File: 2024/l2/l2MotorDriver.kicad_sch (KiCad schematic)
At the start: 17 parts, among them J4 Conn_01x02, J5 Conn_01x02, J6 Conn_01x02, J7 Conn_01x02, Q1 IRF540N, Q2 IRF540N, Q3 IRF540N, Q4 IRF540N, SW1 SW_SPDT, U1 VNH5019A-E, U2 VNH5019A-E, U3 VNH5019A-E, U4 VNH5019A-E

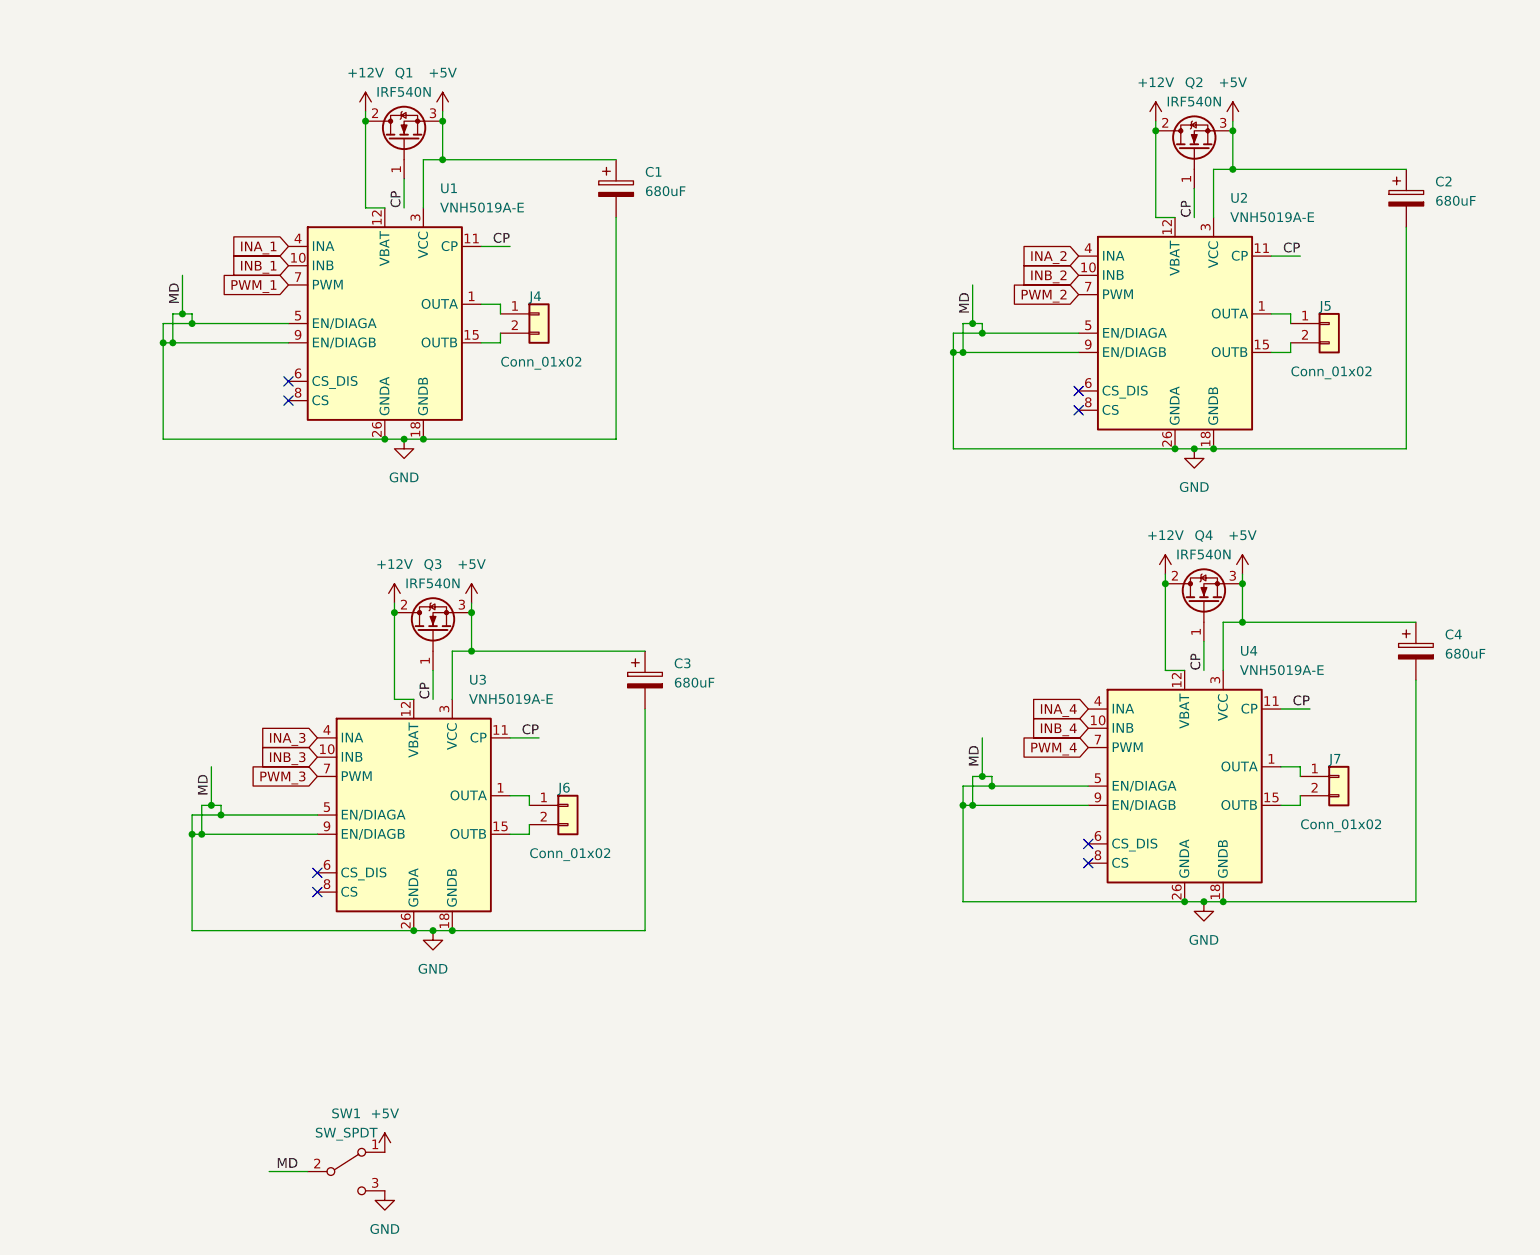
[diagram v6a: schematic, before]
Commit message: 5/9 final
fixed the problem with motor driver schematics
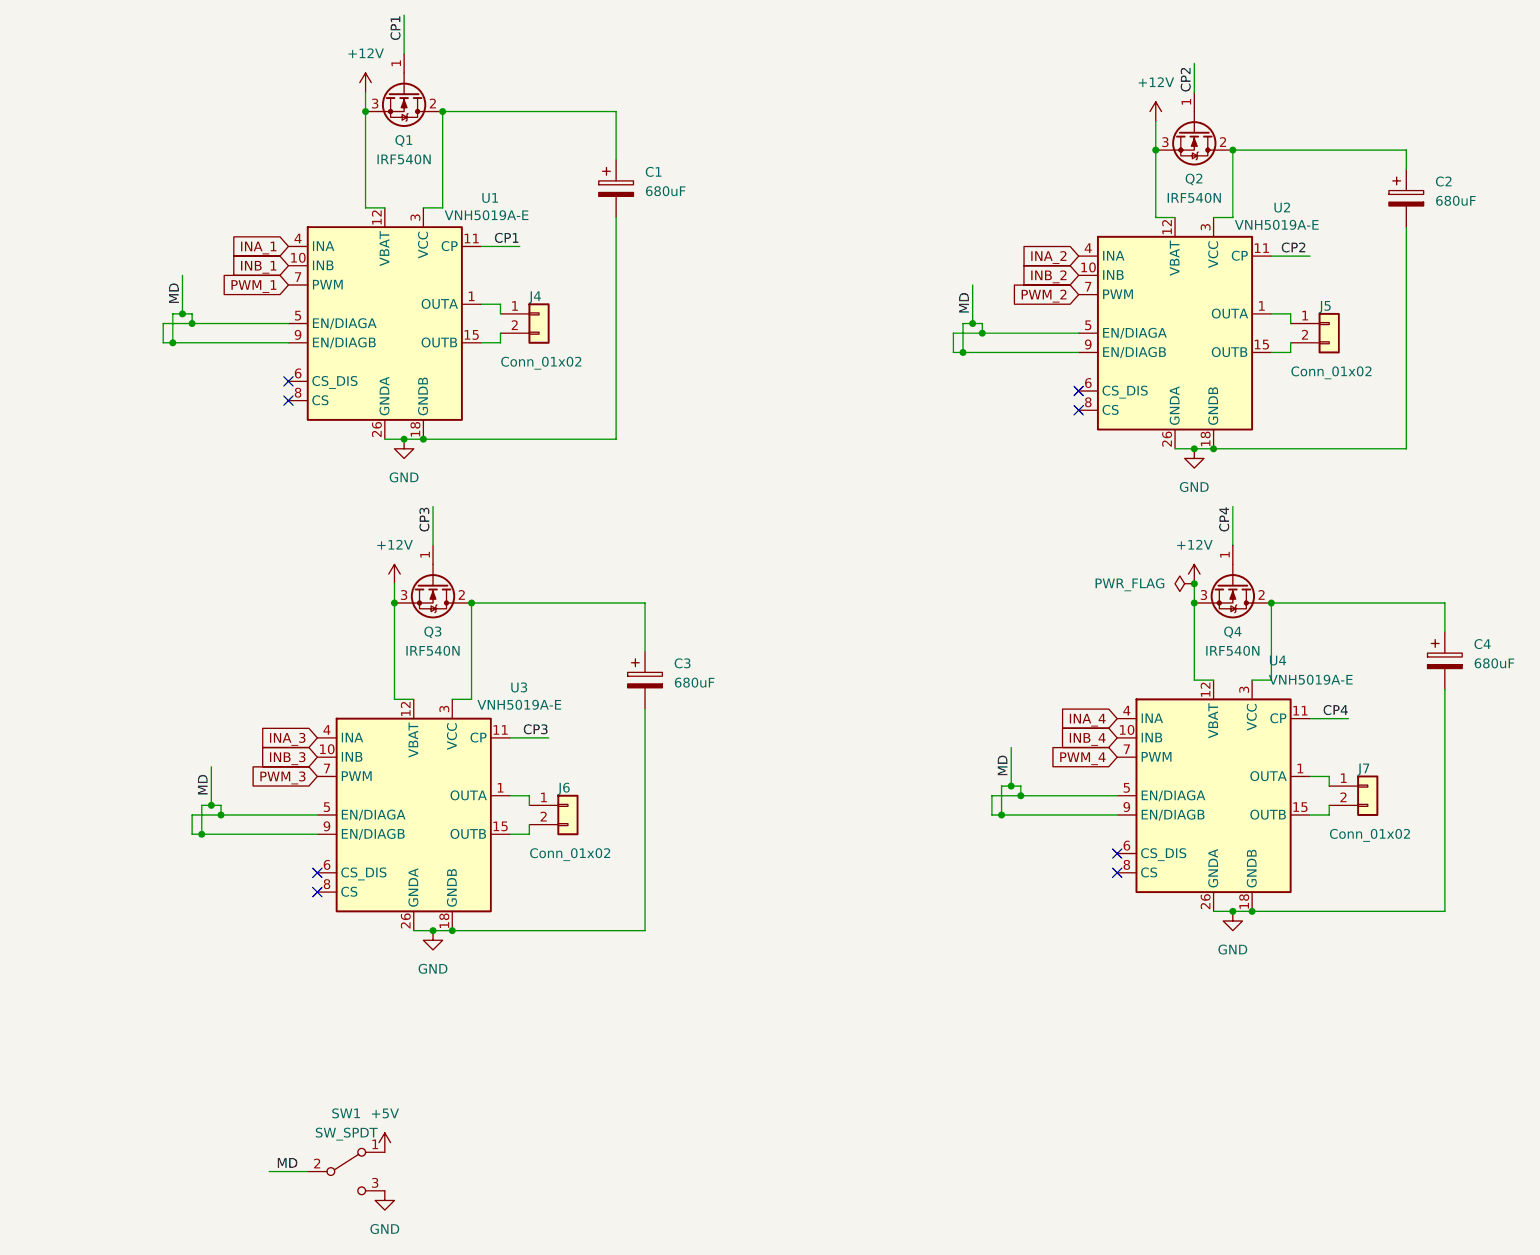
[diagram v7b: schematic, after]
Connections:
- net +12V: now also Q1.3 (S), Q2.3 (S), Q3.3 (S), Q4.3 (S); no longer Q1.2 (D), Q2.2 (D), Q3.2 (D), Q4.2 (D)
- net +5V: no longer C1.1, C2.1, C3.1, C4.1, Q1.3 (S), Q2.3 (S), Q3.3 (S), Q4.3 (S), U1.13 (VCC), U1.23 (VCC), U1.3 (VCC), U1.31 (VCC), U2.13 (VCC), U2.23 (VCC), U2.3 (VCC), U2.31 (VCC), U3.13 (VCC), U3.23 (VCC), U3.3 (VCC), U3.31 (VCC), U4.13 (VCC), U4.23 (VCC), U4.3 (VCC), U4.31 (VCC)
- net GND: no longer SW1.2 (B), U1.5 (EN/DIAGA), U1.9 (EN/DIAGB), U2.5 (EN/DIAGA), U2.9 (EN/DIAGB), U3.5 (EN/DIAGA), U3.9 (EN/DIAGB), U4.5 (EN/DIAGA), U4.9 (EN/DIAGB)
- removed net CP: Q1.1 (G), Q2.1 (G), Q3.1 (G), Q4.1 (G), U1.11 (CP), U2.11 (CP), U3.11 (CP), U4.11 (CP)
- new net: C4.1, Q4.2 (D), U4.13 (VCC), U4.23 (VCC), U4.3 (VCC), U4.31 (VCC)
- new net: C2.1, Q2.2 (D), U2.13 (VCC), U2.23 (VCC), U2.3 (VCC), U2.31 (VCC)
- new net: C1.1, Q1.2 (D), U1.13 (VCC), U1.23 (VCC), U1.3 (VCC), U1.31 (VCC)
- new net: C3.1, Q3.2 (D), U3.13 (VCC), U3.23 (VCC), U3.3 (VCC), U3.31 (VCC)
- new net CP1: Q1.1 (G), U1.11 (CP)
- new net CP2: Q2.1 (G), U2.11 (CP)
- new net CP3: Q3.1 (G), U3.11 (CP)
- new net CP4: Q4.1 (G), U4.11 (CP)
- new net MD: SW1.2 (B), U1.5 (EN/DIAGA), U1.9 (EN/DIAGB), U2.5 (EN/DIAGA), U2.9 (EN/DIAGB), U3.5 (EN/DIAGA), U3.9 (EN/DIAGB), U4.5 (EN/DIAGA), U4.9 (EN/DIAGB)
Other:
- moved on the sheet: C4, J7, Q1, Q2, Q3, Q4, U4

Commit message: final 0.9
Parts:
- added R1: 3.3k, Resistor_SMD:R_0603_1608Metric_Pad0.98x0.95mm_HandSolder, symbol Device:R
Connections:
- net +5V: now also R1.2; no longer SW1.1 (A)
- new net: R1.1, SW1.1 (A)
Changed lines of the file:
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@@
+	)
+	(symbol
+		(lib_id "power:+5V")
+		(at 95.25 172.72 0)
+		(unit 1)
+		(exclude_from_sim no)
+		(in_bom yes)
+		(on_board yes)
+		(dnp no)
+		(fields_autoplaced yes)
+		(property "Reference" "#PWR09"
+			(at 95.25 176.53 0)
+			(effects
+				(font
+					(size 1.27 1.27)
+				)
+				(hide yes)
+			)
+		)
+		(property "Value" "+5V"
+			(at 95.25 167.64 0)
+			(effects
+				(font
+					(size 1.27 1.27)
+				)
+			)
+		)
+		(property "Footprint" ""
+			(at 95.25 172.72 0)
+			(effects
+				(font
+					(size 1.27 1.27)
+				)
+				(hide yes)
+			)
+		)
+		(property "Datasheet" ""
+			(at 95.25 172.72 0)
+			(effects
+				(font
+					(size 1.27 1.27)
+				)
+				(hide yes)
+			)
+		)
+		(property "Description" "Power symbol creates a global label with name \"+5V\""
+			(at 95.25 172.72 0)
+			(effects
+				(font
+					(size 1.27 1.27)
+				)
+				(hide yes)
+			)
+		)
+		(pin "1"
+		)
+		(instances
+			(project ""
+				(path "/6e23b0dc-b56a-4591-91ab-7fa94dae0df0/07f2b048-6ef5-43cf-a929-1dfccb679372"
+					(reference "#PWR09")
+					(unit 1)
+				)
+			)
+		)
 	)
 	(symbol
@@
 	)
 	(symbol
-		(lib_id "power:+5V")
-		(at 87.63 172.72 0)
-		(unit 1)
-		(exclude_from_sim no)
-		(in_bom yes)
-		(on_board yes)
-		(dnp no)
-		(fields_autoplaced yes)
-		(property "Reference" "#PWR09"
-			(at 87.63 176.53 0)
-			(effects
-				(font
-					(size 1.27 1.27)
-				)
-				(hide yes)
-			)
-		)
-		(property "Value" "+5V"
-			(at 87.63 167.64 0)
-			(effects
-				(font
-					(size 1.27 1.27)
-				)
-			)
-		)
-		(property "Footprint" ""
-			(at 87.63 172.72 0)
-			(effects
-				(font
-					(size 1.27 1.27)
-				)
-				(hide yes)
-			)
-		)
-		(property "Datasheet" ""
-			(at 87.63 172.72 0)
-			(effects
-				(font
-					(size 1.27 1.27)
-				)
-				(hide yes)
-			)
-		)
-		(property "Description" "Power symbol creates a global label with name \"+5V\""
-			(at 87.63 172.72 0)
-			(effects
-				(font
-					(size 1.27 1.27)
-				)
-				(hide yes)
-			)
-		)
-		(pin "1"
-		)
-		(instances
-			(project "l2"
-				(path "/6e23b0dc-b56a-4591-91ab-7fa94dae0df0/07f2b048-6ef5-43cf-a929-1dfccb679372"
-					(reference "#PWR09")
-					(unit 1)
-				)
-			)
-		)
-	)
-	(symbol
 		(lib_id "Connector_Generic:Conn_01x02")
 		(at 107.95 62.23 0)
@@
 					(unit 1)
 				)
+			)
+		)
+	)
+	(symbol
+		(lib_id "Device:R")
+		(at 91.44 172.72 90)
+		(unit 1)
+		(exclude_from_sim no)
+		(in_bom yes)
+		(on_board yes)
+		(dnp no)
+		(fields_autoplaced yes)
+		(property "Reference" "R1"
+			(at 91.44 166.37 90)
+			(effects
+				(font
+					(size 1.27 1.27)
+				)
+			)
+		)
+		(property "Value" "3.3k"
+			(at 91.44 168.91 90)
+			(effects
+				(font
+					(size 1.27 1.27)
+				)
+			)
+		)
+		(property "Footprint" "Resistor_SMD:R_0603_1608Metric_Pad0.98x0.95mm_HandSolder"
+			(at 91.44 174.498 90)
+			(effects
+				(font
+					(size 1.27 1.27)
+				)
+				(hide yes)
+			)
+		)
+		(property "Datasheet" "~"
+			(at 91.44 172.72 0)
+			(effects
+				(font
+					(size 1.27 1.27)
+				)
+				(hide yes)
+			)
+		)
+		(property "Description" "Resistor"
+			(at 91.44 172.72 0)
+			(effects
+				(font
+					(size 1.27 1.27)
+				)
+				(hide yes)
+			)
+		)
+		(pin "1"
+		)
+		(pin "2"
+		)
+		(instances
+			(project ""
+				(path "/6e23b0dc-b56a-4591-91ab-7fa94dae0df0/07f2b048-6ef5-43cf-a929-1dfccb679372"
+					(reference "R1")
+					(unit 1)
+				)
